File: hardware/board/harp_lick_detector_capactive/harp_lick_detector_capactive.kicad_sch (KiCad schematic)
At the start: 48 parts, among them J1 3-Pin Connector Socket, J3 Conn_Coaxial, J4 Conn_Coaxial, J5 Barrel_Jack_Switch_Pin3Ring, U1 INA849, U2 ADA4807-4, U5 LT3030, U6 LM27762

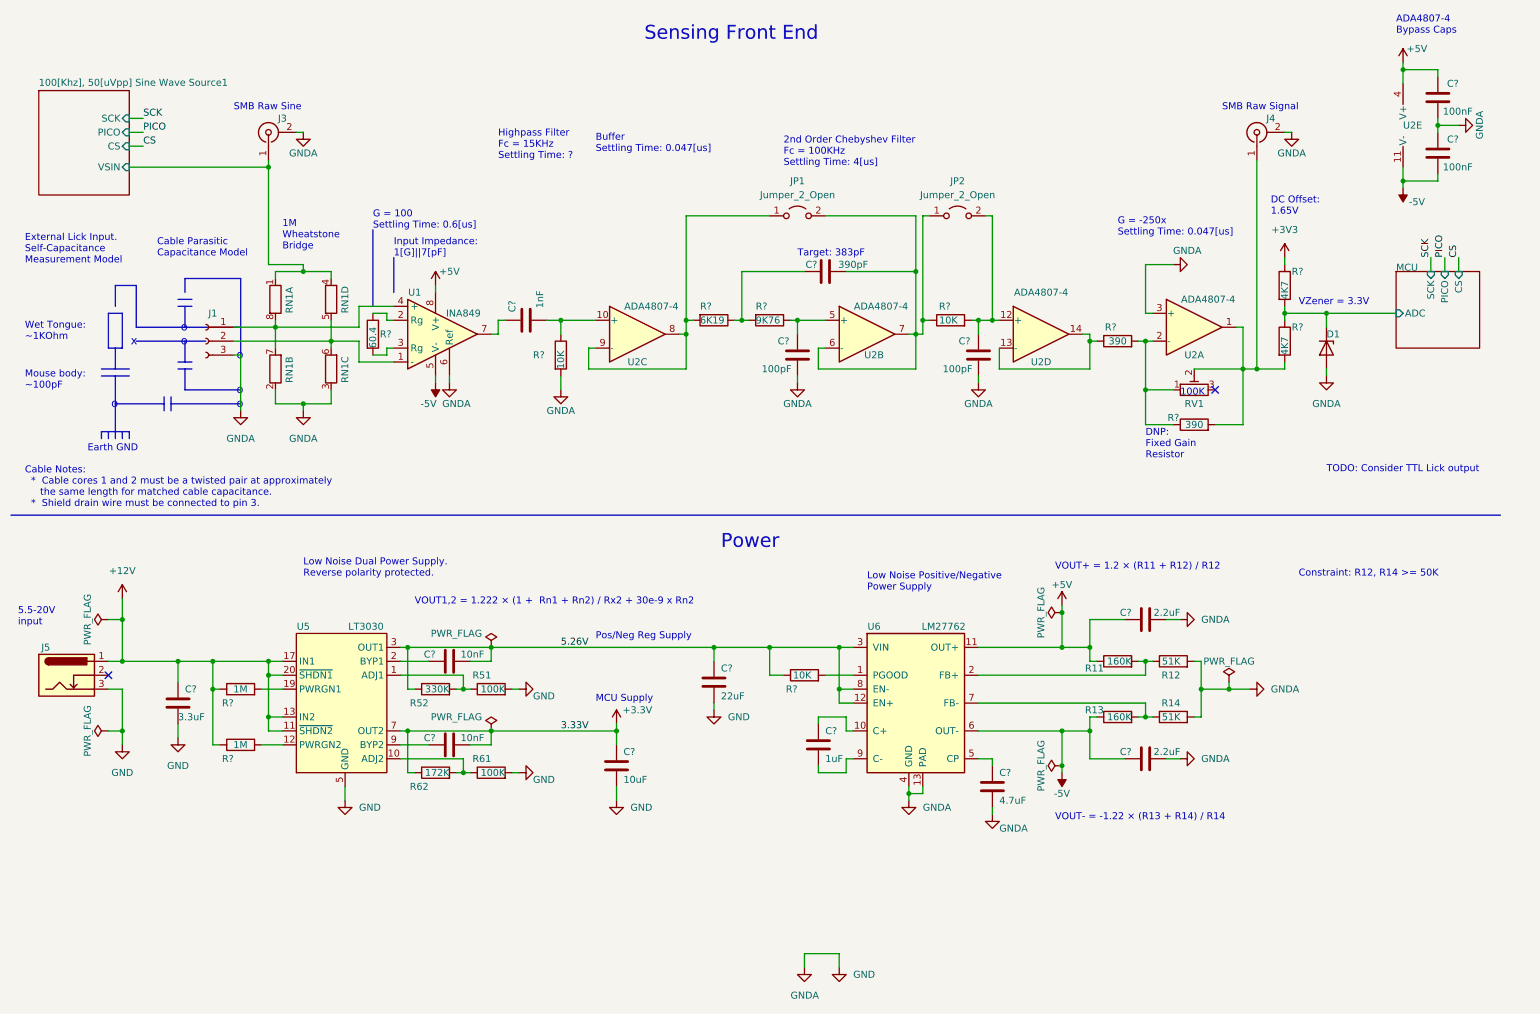
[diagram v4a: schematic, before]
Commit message: add ttl output; update adc voltage
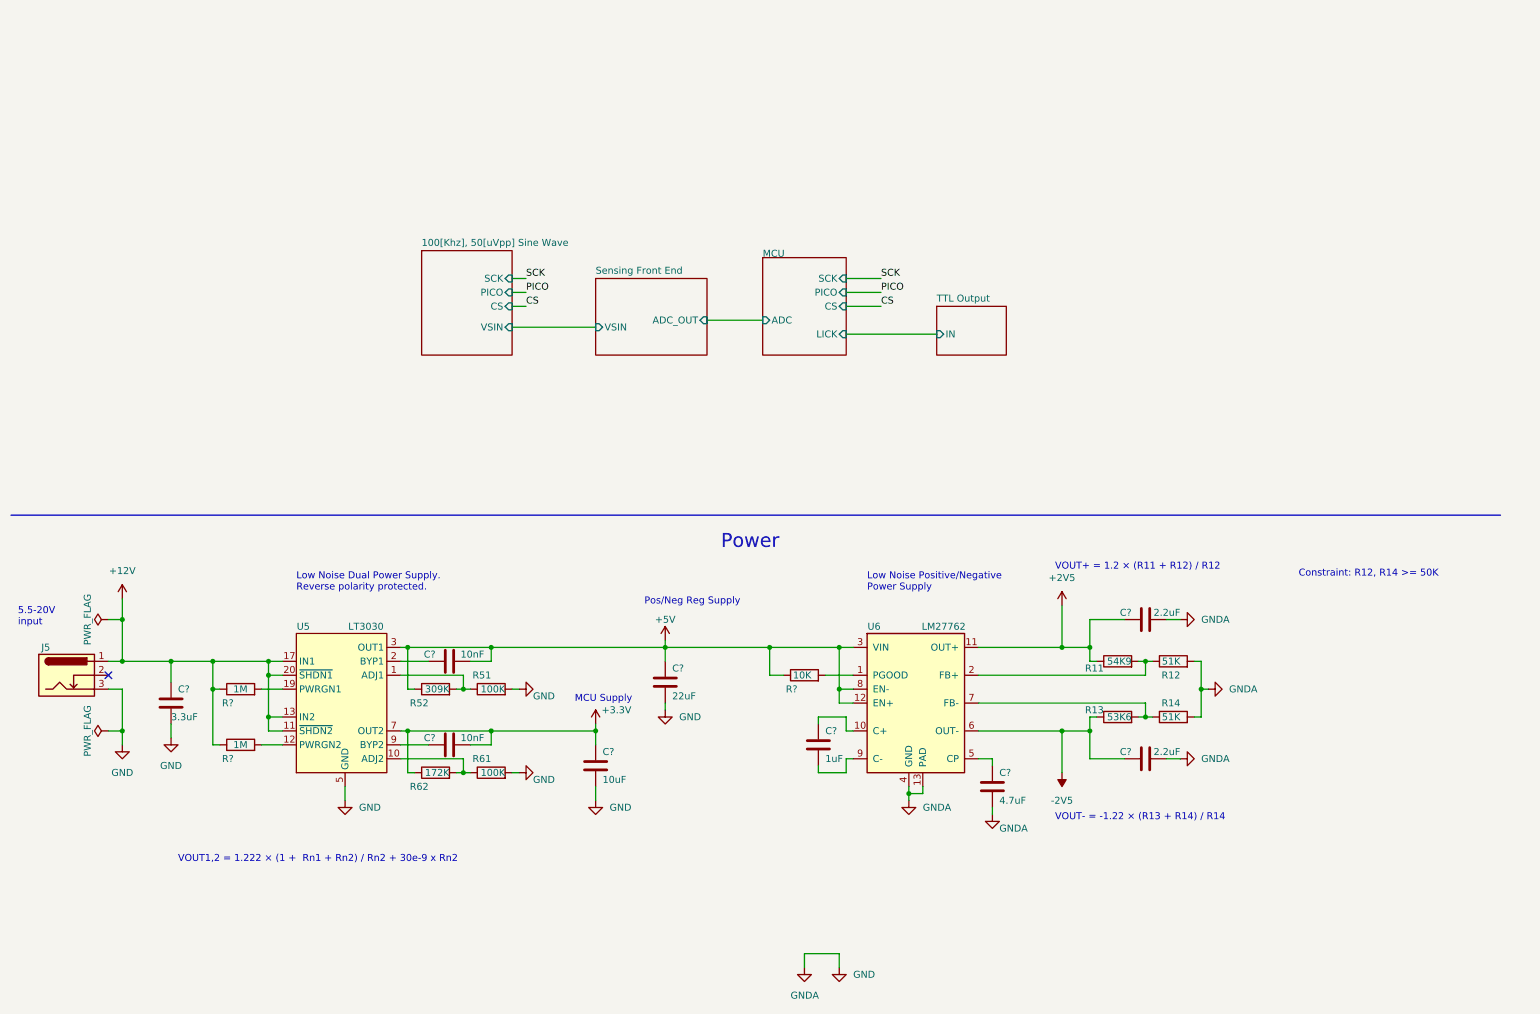
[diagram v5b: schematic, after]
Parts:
- removed C? (x2): 100nF, Capacitor_SMD:C_0603_1608Metric_Pad1.08x0.95mm_HandSolder, symbol Device:C
- removed C?: 1nF, Capacitor_SMD:C_0603_1608Metric_Pad1.08x0.95mm_HandSolder, symbol Device:C
- removed C? (x2): 100pF, Capacitor_SMD:C_0603_1608Metric_Pad1.08x0.95mm_HandSolder, symbol Device:C
- removed C?: 390pF, Resistor_SMD:R_0402_1005Metric_Pad0.72x0.64mm_HandSolder, symbol Device:C
- removed D1: BZX384-A3V3-QX, Diode_SMD:D_SOD-323_HandSoldering, symbol Diode:BZV55B3V3
- removed J1: 3-Pin Connector Socket, Connector_Phoenix_MC:PhoenixContact_MC_1,5_3-G-3.5_1x03_P3.50mm_Horizontal, symbol Connector:Conn_01x03_Female
- removed J3, J4: Conn_Coaxial, Connector_Coaxial:SMA_Amphenol_901-143_Horizontal, symbol Connector:Conn_Coaxial
- removed JP1, JP2: Jumper_2_Open, Jumper:SolderJumper-2_P1.3mm_Open_RoundedPad1.0x1.5mm, symbol Jumper:Jumper_2_Open
- removed R? (x2): 10K, Resistor_SMD:R_0402_1005Metric_Pad0.72x0.64mm_HandSolder, symbol Device:R
- removed R?: 6K19, Resistor_SMD:R_0603_1608Metric_Pad0.98x0.95mm_HandSolder, symbol Device:R
- removed R?: 9K76, Resistor_SMD:R_0603_1608Metric_Pad0.98x0.95mm_HandSolder, symbol Device:R
- removed R? (x2): 390, Resistor_SMD:R_0603_1608Metric_Pad0.98x0.95mm_HandSolder, symbol Device:R
- removed R? (x2): 4K7, Resistor_SMD:R_0603_1608Metric_Pad0.98x0.95mm_HandSolder, symbol Device:R
- removed R?: 60.4, Resistor_SMD:R_0603_1608Metric_Pad0.98x0.95mm_HandSolder, symbol Device:R
- removed RN1: R_Pack04_Split, Package_SO:MSOP-8_3x3mm_P0.65mm, symbol Device:R_Pack04_Split
- removed RV1: R_Potentiometer_Trim, Potentiometer_SMD:Potentiometer_Bourns_3314G_Vertical, symbol Device:R_Potentiometer_Trim
- removed U1: INA849, Package_SO:SOIC-8-1EP_3.9x4.9mm_P1.27mm_EP2.29x3mm, symbol machine_agency_components:INA849
- removed U2: ADA4807-4, Package_SO:TSSOP-14_4.4x5mm_P0.65mm, symbol Amplifier_Operational:ADA4807-4
- R11: value 160K -> 54K9; Link https://www.digikey.com/en/products/detail/panasonic-electr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 -> https://www.digikey.com/en/products/detail/yageo/RC0603FR-0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; Manufacturer Panasonic Electronic Components -> Yageo; Manufacturer Number ERJ-UP3F1603V -> RC0603FR-0754K9L
- R13: value 160K -> 53K6; Link https://www.digikey.com/en/products/detail/panasonic-electr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 -> https://www.digikey.com/en/products/detail/yageo/RC0603FR-0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; Manufacturer Panasonic Electronic Components -> Yageo; Manufacturer Number ERJ-UP3F1603V -> RC0603FR-0753K6L
- R52: value 330K -> 309K; Link https://www.digikey.com/en/products/detail/te-connectivity-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 -> https://www.digikey.com/en/products/detail/yageo/RC0603FR-0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; Manufacturer TE Connectivity Passive Product -> Yageo; Manufacturer Number CRGP0603F330K -> RC0603FR-07309RL
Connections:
- net 5.26V is gone; now on net +5V: C?.1, C?.2, R52.1, R?.1, U5.3 (OUT1), U5.4 (OUT1), U6.12 (EN+), U6.3 (VIN), U6.8 (EN-)
- net +5V: no longer C?.1, R11.1, U6.11 (OUT+)
- net -5V renamed -2V5
- new net +2V5: C?.1, R11.1, U6.11 (OUT+)
- no-connect marks 2 -> 1
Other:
- sheet 100[Khz], 50[uVpp] Sine Wave Source1 renamed 100[Khz], 50[uVpp] Sine Wave
- added sheet Sensing Front End (sensing_front_end.kicad_sch)
- added sheet TTL Output (ttl_output.kicad_sch)
- sheet MCU ports: added LICK; removed none
- note added: "VOUT1,2 = 1.222 × (1 + Rn1 + Rn2) / Rn2 + 30e-9 x Rn2"
- note removed: "100K"
- note removed: "1M Wheatstone Bridge"
- note removed: "2nd Order Chebyshev Filter Fc = 100KHz Settling Time: 4[us]"
- note removed: "ADA4807-4 Bypass Caps"
- note removed: "Buffer Settling Time: 0.047[us]"
- note removed: "Cable Notes: * Cable cores 1 and 2 must be a twisted pair at approximately the same length for matched cable capacitance. * Shield drain wire must be connected to pin 3."
- note removed: "Cable Parasitic Capacitance Model"
- note removed: "DC Offset: 1.65V"
- note removed: "DNP: Fixed Gain Resistor"
- note removed: "Earth GND"
- note removed: "External Lick Input. Self-Capacitance Measurement Model"
- note removed: "G = -250x Settling Time: 0.047[us]"
- note removed: "G = 100 Settling Time: 0.6[us]"
- note removed: "Highpass Filter Fc = 15KHz Settling Time: ?"
- note removed: "Input Impedance: 1[G]||7[pF]"
- note removed: "Mouse body: ~100pF"
- note removed: "SMB Raw Signal"
- note removed: "SMB Raw Sine"
- note removed: "Sensing Front End"
- note removed: "TODO: Consider TTL Lick output"
- note removed: "Target: 383pF"
- note removed: "VOUT1,2 = 1.222 × (1 + Rn1 + Rn2) / Rx2 + 30e-9 x Rn2"
- note removed: "VZener = 3.3V"
- note removed: "Wet Tongue: ~1KOhm"
- note removed: "o"
- note removed: "x"
- moved on the sheet: C?

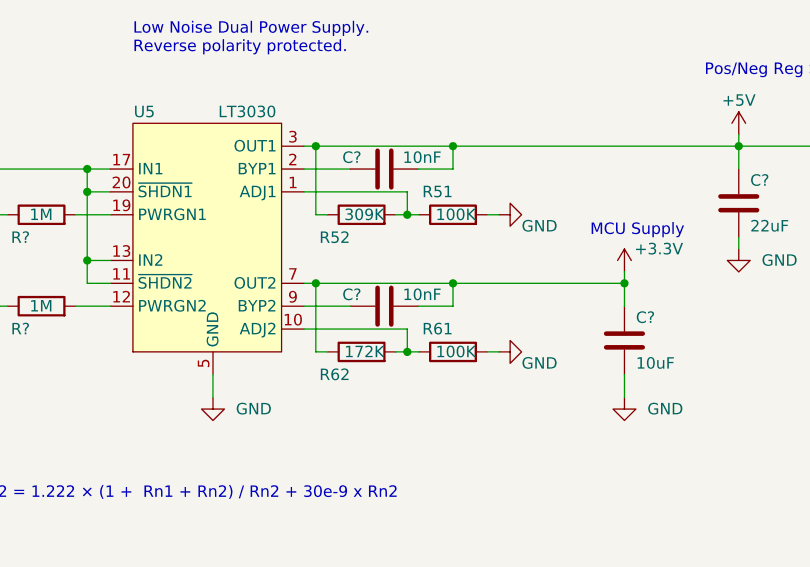
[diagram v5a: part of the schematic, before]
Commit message: update resistor value from 309 to 309K
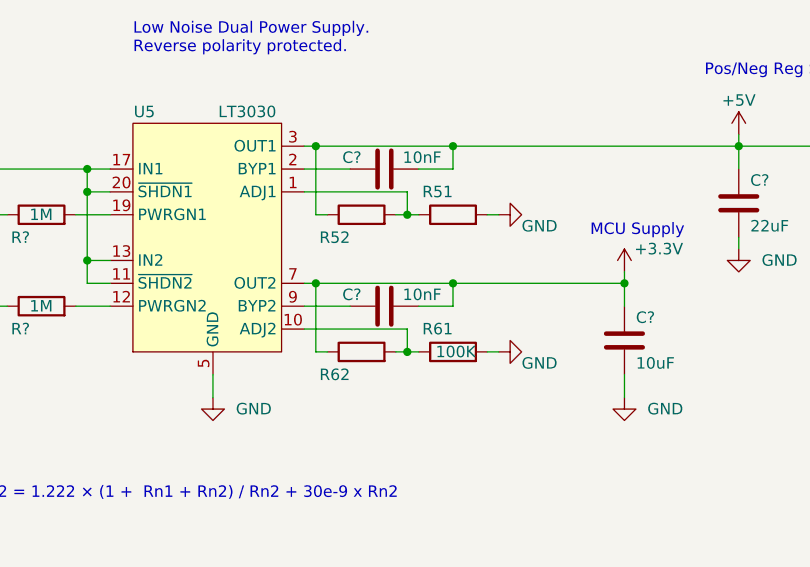
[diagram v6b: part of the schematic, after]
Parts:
- R51: value 100K -> (none); footprint Capacitor_SMD:C_0603_1608Metric_Pad1.08x0.95mm_HandSolder -> (none)
- R52: value 309K -> (none); footprint Resistor_SMD:R_0603_1608Metric_Pad0.98x0.95mm_HandSolder -> (none); Link https://www.digikey.com/en/products/detail/yageo/RC0603FR-07309RL/727148 -> https://www.digikey.com/en/products/detail/yageo/RC0603FR-07309KL/727149; Manufacturer Number RC0603FR-07309RL -> RC0603FR-07309KL
- R62: value 172K -> (none); footprint Resistor_SMD:R_0603_1608Metric_Pad0.98x0.95mm_HandSolder -> (none)
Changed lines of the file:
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@@
       (effects (font (size 1.27 1.27)) (justify left))
     )
-    (property "Value" "309K" (id 1) (at 92.71 137.16 90)
-      (effects (font (size 1.27 1.27)) (justify left))
-    )
-    (property "Footprint" "Resistor_SMD:R_0603_1608Metric_Pad0.98x0.95mm_HandSolder" (id 2) (at 90.17 138.938 90)
+    (property "Value" "" (id 1) (at 92.71 137.16 90)
+      (effects (font (size 1.27 1.27)) (justify left))
+    )
+    (property "Footprint" "" (id 2) (at 90.17 138.938 90)
       (effects (font (size 1.27 1.27)) hide)
     )
@@
       (effects (font (size 1.27 1.27)) hide)
     )
-    (property "Link" "https://www.digikey.com/en/products/detail/yageo/RC0603FR-07309RL/727148" (id 4) (at 90.17 137.16 90)
+    (property "Link" "https://www.digikey.com/en/products/detail/yageo/RC0603FR-07309KL/727149" (id 4) (at 90.17 137.16 90)
       (effects (font (size 1.27 1.27)) hide)
     )
@@
       (effects (font (size 1.27 1.27)) hide)
     )
-    (property "Manufacturer Number" "RC0603FR-07309RL" (id 6) (at 90.17 137.16 0)
+    (property "Manufacturer Number" "RC0603FR-07309KL" (id 6) (at 90.17 137.16 0)
       (effects (font (size 1.27 1.27)) hide)
     )
@@
       (effects (font (size 1.27 1.27)) (justify left))
     )
-    (property "Value" "172K" (id 1) (at 92.71 152.4 90)
-      (effects (font (size 1.27 1.27)) (justify left))
-    )
-    (property "Footprint" "Resistor_SMD:R_0603_1608Metric_Pad0.98x0.95mm_HandSolder" (id 2) (at 90.17 154.178 90)
+    (property "Value" "" (id 1) (at 92.71 152.4 90)
+      (effects (font (size 1.27 1.27)) (justify left))
+    )
+    (property "Footprint" "" (id 2) (at 90.17 154.178 90)
       (effects (font (size 1.27 1.27)) hide)
     )
@@
       (effects (font (size 1.27 1.27)) (justify left))
     )
-    (property "Value" "100K" (id 1) (at 102.87 137.16 90)
-      (effects (font (size 1.27 1.27)) (justify left))
-    )
-    (property "Footprint" "Capacitor_SMD:C_0603_1608Metric_Pad1.08x0.95mm_HandSolder" (id 2) (at 100.33 138.938 90)
-      (effects (font (size 1.27 1.27)) hide)
-    )
+    (property "Value" "" (id 1) (at 102.87 137.16 90)
+      (effects (font (size 1.27 1.27)) (justify left))
+    )
+    (property "Footprint" "" (id 2) (at 100.33 138.938 90)
+      (effects (font (size 1.27 1.27)) hide)
+    )

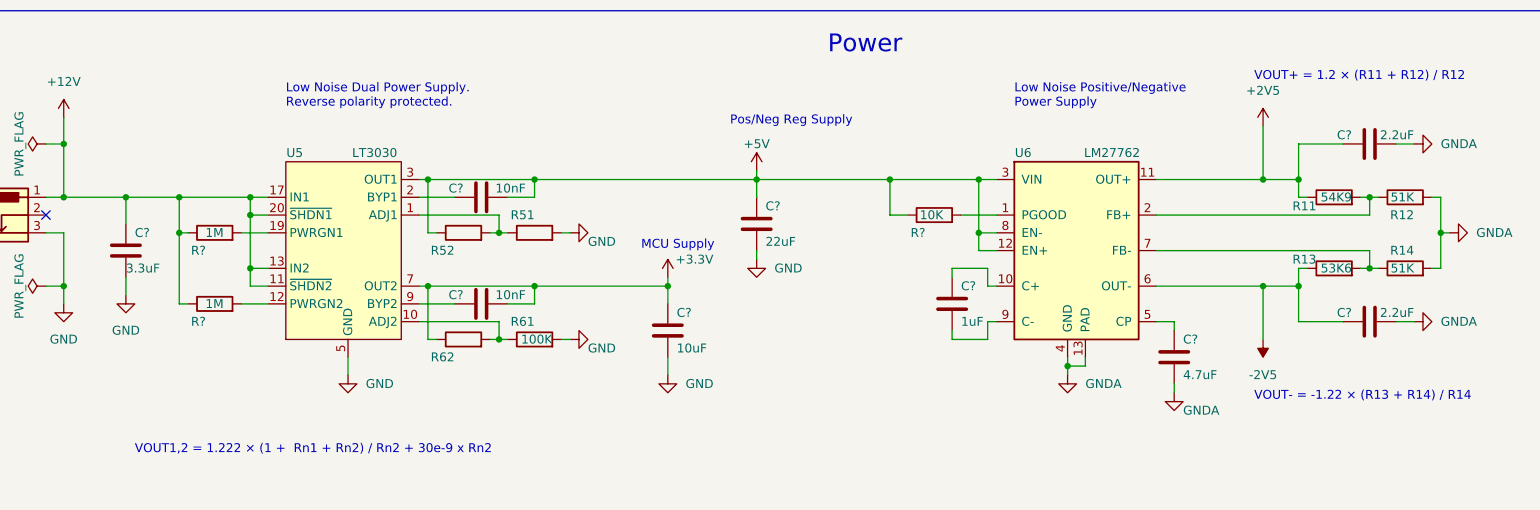
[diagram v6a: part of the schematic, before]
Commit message: add extra series termination resistors
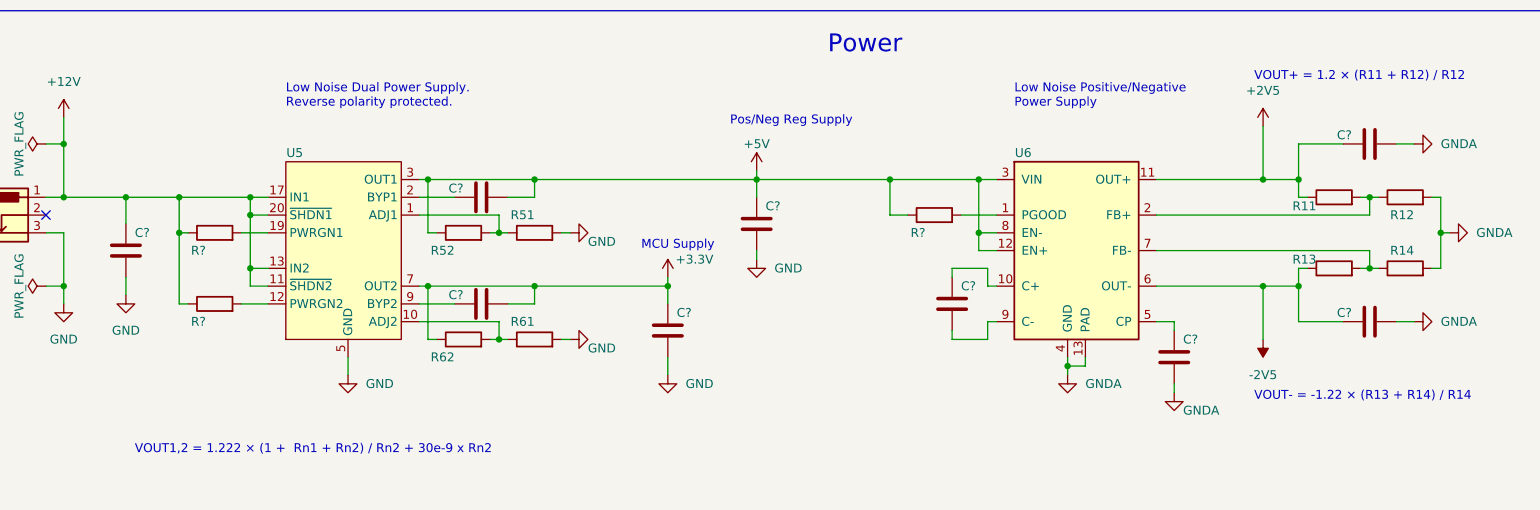
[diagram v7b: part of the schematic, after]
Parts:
- C?: value 1uF -> (none); footprint Capacitor_SMD:C_0603_1608Metric_Pad1.08x0.95mm_HandSolder -> (none)
- C?: value 3.3uF -> (none); footprint Capacitor_SMD:C_0805_2012Metric_Pad1.18x1.45mm_HandSolder -> (none)
- C?: value 22uF -> (none); footprint Capacitor_SMD:C_0805_2012Metric_Pad1.18x1.45mm_HandSolder -> (none)
- C? (x2): value 2.2uF -> (none); footprint Capacitor_SMD:C_0603_1608Metric_Pad1.08x0.95mm_HandSolder -> (none)
- C?: value 10uF -> (none); footprint Capacitor_SMD:C_0805_2012Metric -> (none)
- C?: value 4.7uF -> (none); footprint Capacitor_SMD:C_0805_2012Metric_Pad1.18x1.45mm_HandSolder -> (none)
- C? (x2): value 10nF -> (none); footprint Capacitor_SMD:C_0603_1608Metric_Pad1.08x0.95mm_HandSolder -> (none)
- J5: value Barrel_Jack_Switch_Pin3Ring -> (none)
- R11: value 54K9 -> (none); footprint Resistor_SMD:R_0603_1608Metric_Pad0.98x0.95mm_HandSolder -> (none)
- R12, R14: value 51K -> (none); footprint Resistor_SMD:R_0603_1608Metric_Pad0.98x0.95mm_HandSolder -> (none)
- R13: value 53K6 -> (none); footprint Resistor_SMD:R_0603_1608Metric_Pad0.98x0.95mm_HandSolder -> (none)
- R61: value 100K -> (none); footprint Capacitor_SMD:C_0603_1608Metric_Pad1.08x0.95mm_HandSolder -> (none)
- R?: value 10K -> (none); footprint Resistor_SMD:R_0402_1005Metric_Pad0.72x0.64mm_HandSolder -> (none)
- R? (x2): value 1M -> (none); footprint Resistor_SMD:R_0603_1608Metric_Pad0.98x0.95mm_HandSolder -> (none)
- U5: value LT3030 -> (none); footprint Package_SO:TSSOP-20_4.4x6.5mm_P0.65mm -> (none)
- U6: value LM27762 -> (none); footprint Package_SON:WSON-12-1EP_3x2mm_P0.5mm_EP1x2.65_ThermalVias -> (none)

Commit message: add driven shield
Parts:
- C?: value (none) -> 1uF; footprint (none) -> Capacitor_SMD:C_0603_1608Metric_Pad1.08x0.95mm_HandSolder
- C?: value (none) -> 3.3uF; footprint (none) -> Capacitor_SMD:C_0805_2012Metric_Pad1.18x1.45mm_HandSolder
- C?: value (none) -> 22uF; footprint (none) -> Capacitor_SMD:C_0805_2012Metric_Pad1.18x1.45mm_HandSolder
- C? (x2): value (none) -> 2.2uF; footprint (none) -> Capacitor_SMD:C_0603_1608Metric_Pad1.08x0.95mm_HandSolder
- C?: value (none) -> 10uF; footprint (none) -> Capacitor_SMD:C_0805_2012Metric
- C?: value (none) -> 4.7uF; footprint (none) -> Capacitor_SMD:C_0805_2012Metric_Pad1.18x1.45mm_HandSolder
- C? (x2): value (none) -> 10nF; footprint (none) -> Capacitor_SMD:C_0603_1608Metric_Pad1.08x0.95mm_HandSolder
- J5: value (none) -> Barrel_Jack_Switch_Pin3Ring
- R11: value (none) -> 54K9; footprint (none) -> Resistor_SMD:R_0603_1608Metric_Pad0.98x0.95mm_HandSolder
- R12, R14: value (none) -> 51K; footprint (none) -> Resistor_SMD:R_0603_1608Metric_Pad0.98x0.95mm_HandSolder
- R13: value (none) -> 53K6; footprint (none) -> Resistor_SMD:R_0603_1608Metric_Pad0.98x0.95mm_HandSolder
- R51, R61: value (none) -> 100K; footprint (none) -> Capacitor_SMD:C_0603_1608Metric_Pad1.08x0.95mm_HandSolder
- R52: value (none) -> 309K; footprint (none) -> Resistor_SMD:R_0603_1608Metric_Pad0.98x0.95mm_HandSolder
- R62: value (none) -> 172K; footprint (none) -> Resistor_SMD:R_0603_1608Metric_Pad0.98x0.95mm_HandSolder
- R?: value (none) -> 10K; footprint (none) -> Resistor_SMD:R_0402_1005Metric_Pad0.72x0.64mm_HandSolder
- R? (x2): value (none) -> 1M; footprint (none) -> Resistor_SMD:R_0603_1608Metric_Pad0.98x0.95mm_HandSolder
- U5: value (none) -> LT3030; footprint (none) -> Package_SO:TSSOP-20_4.4x6.5mm_P0.65mm
- U6: value (none) -> LM27762; footprint (none) -> Package_SON:WSON-12-1EP_3x2mm_P0.5mm_EP1x2.65_ThermalVias
